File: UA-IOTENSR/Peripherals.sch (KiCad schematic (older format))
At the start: 4 parts, among them IC1 LM3914VX_NOPB, U4 SCD4X

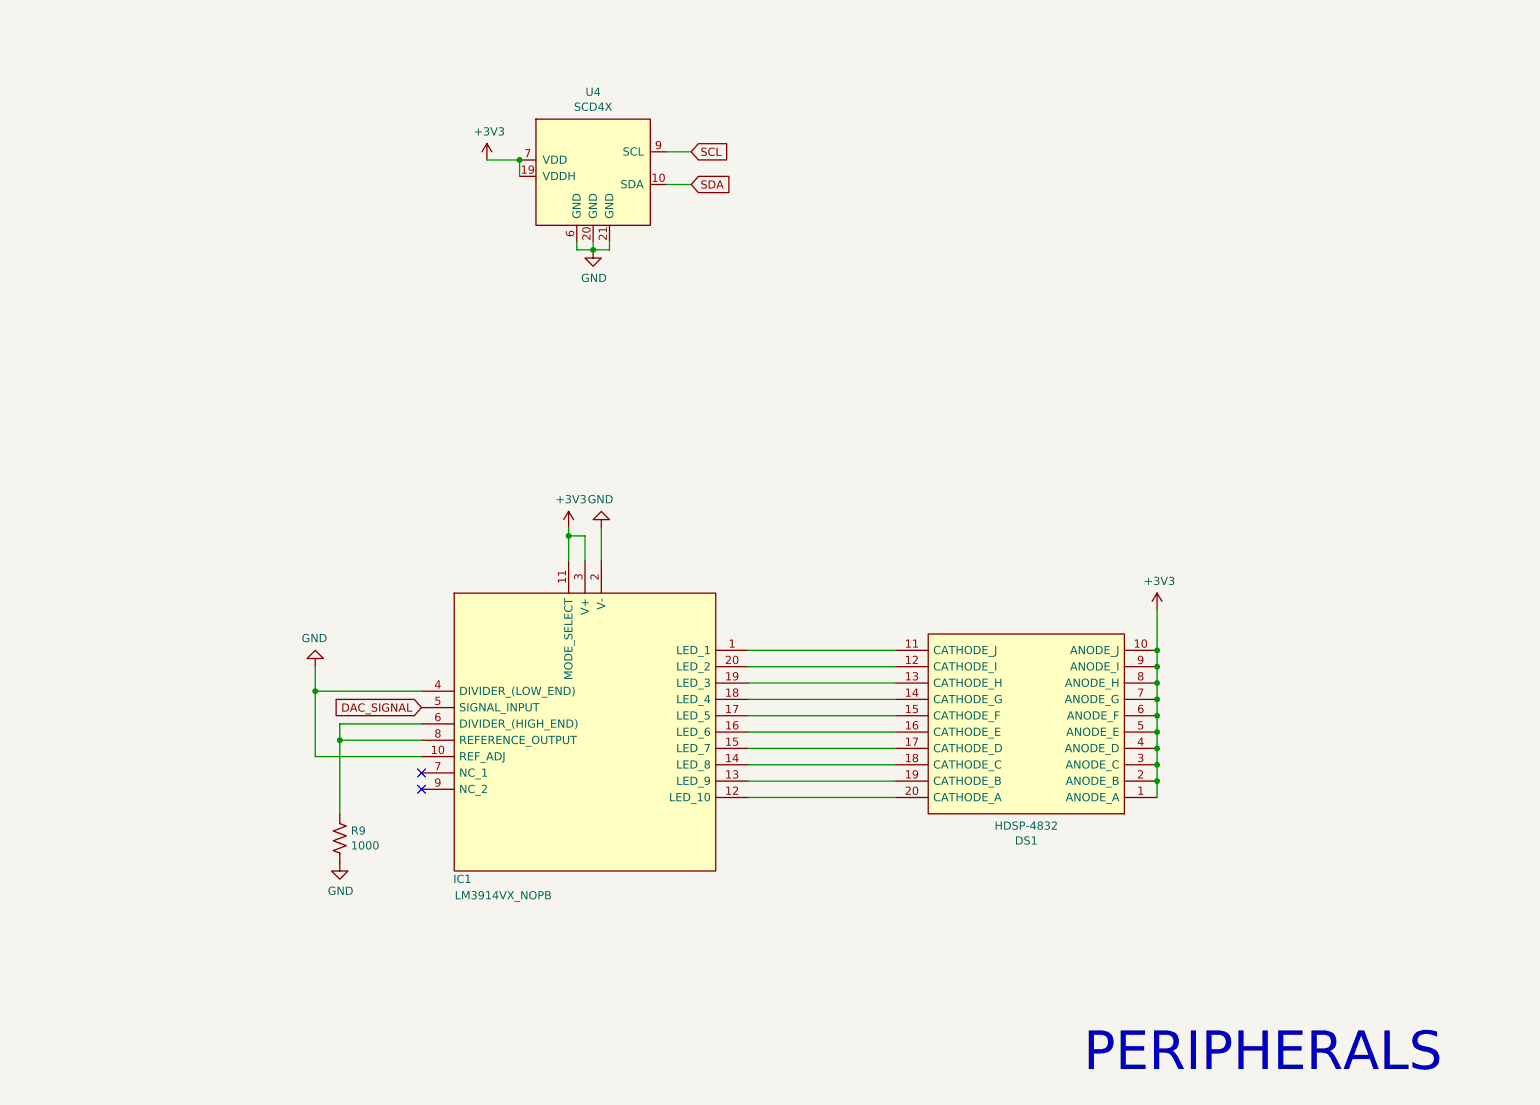
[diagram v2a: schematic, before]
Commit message: Made Peripheral sheet more pretty
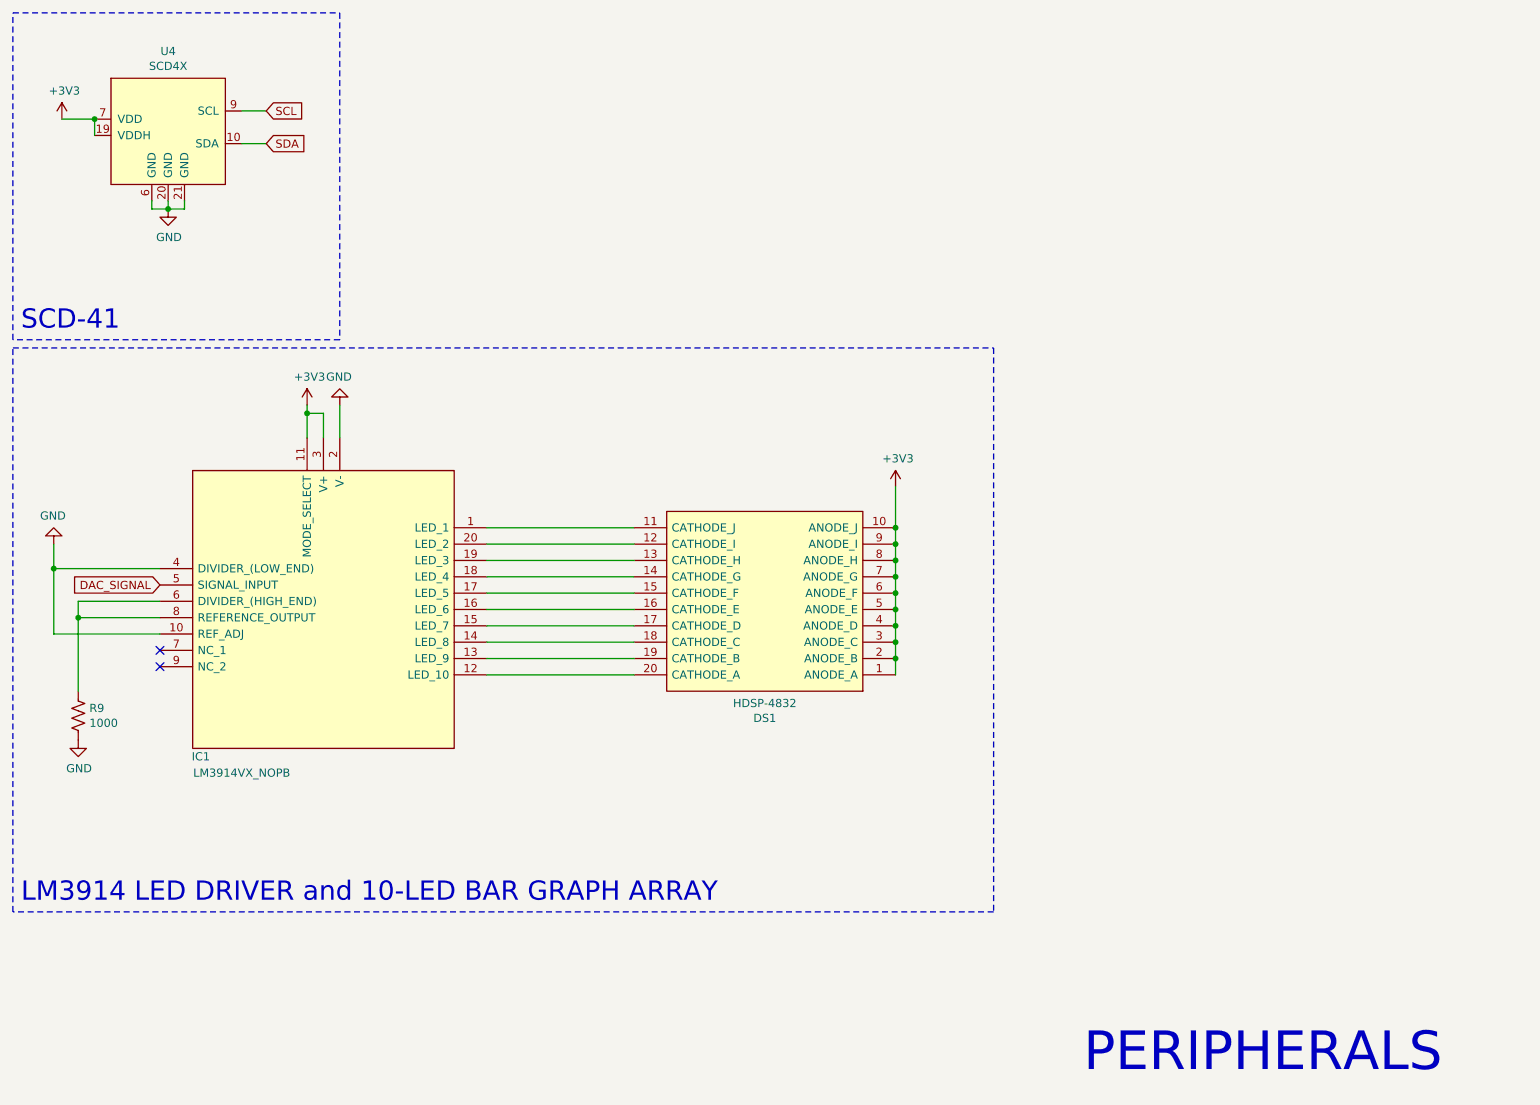
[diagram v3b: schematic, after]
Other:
- note added: "LM3914 LED DRIVER and 10-LED BAR GRAPH ARRAY"
- note added: "SCD-41"
- moved on the sheet: DS1, IC1, R9, U4

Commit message: Reassessed components
Removed bar graph led array and lm3914
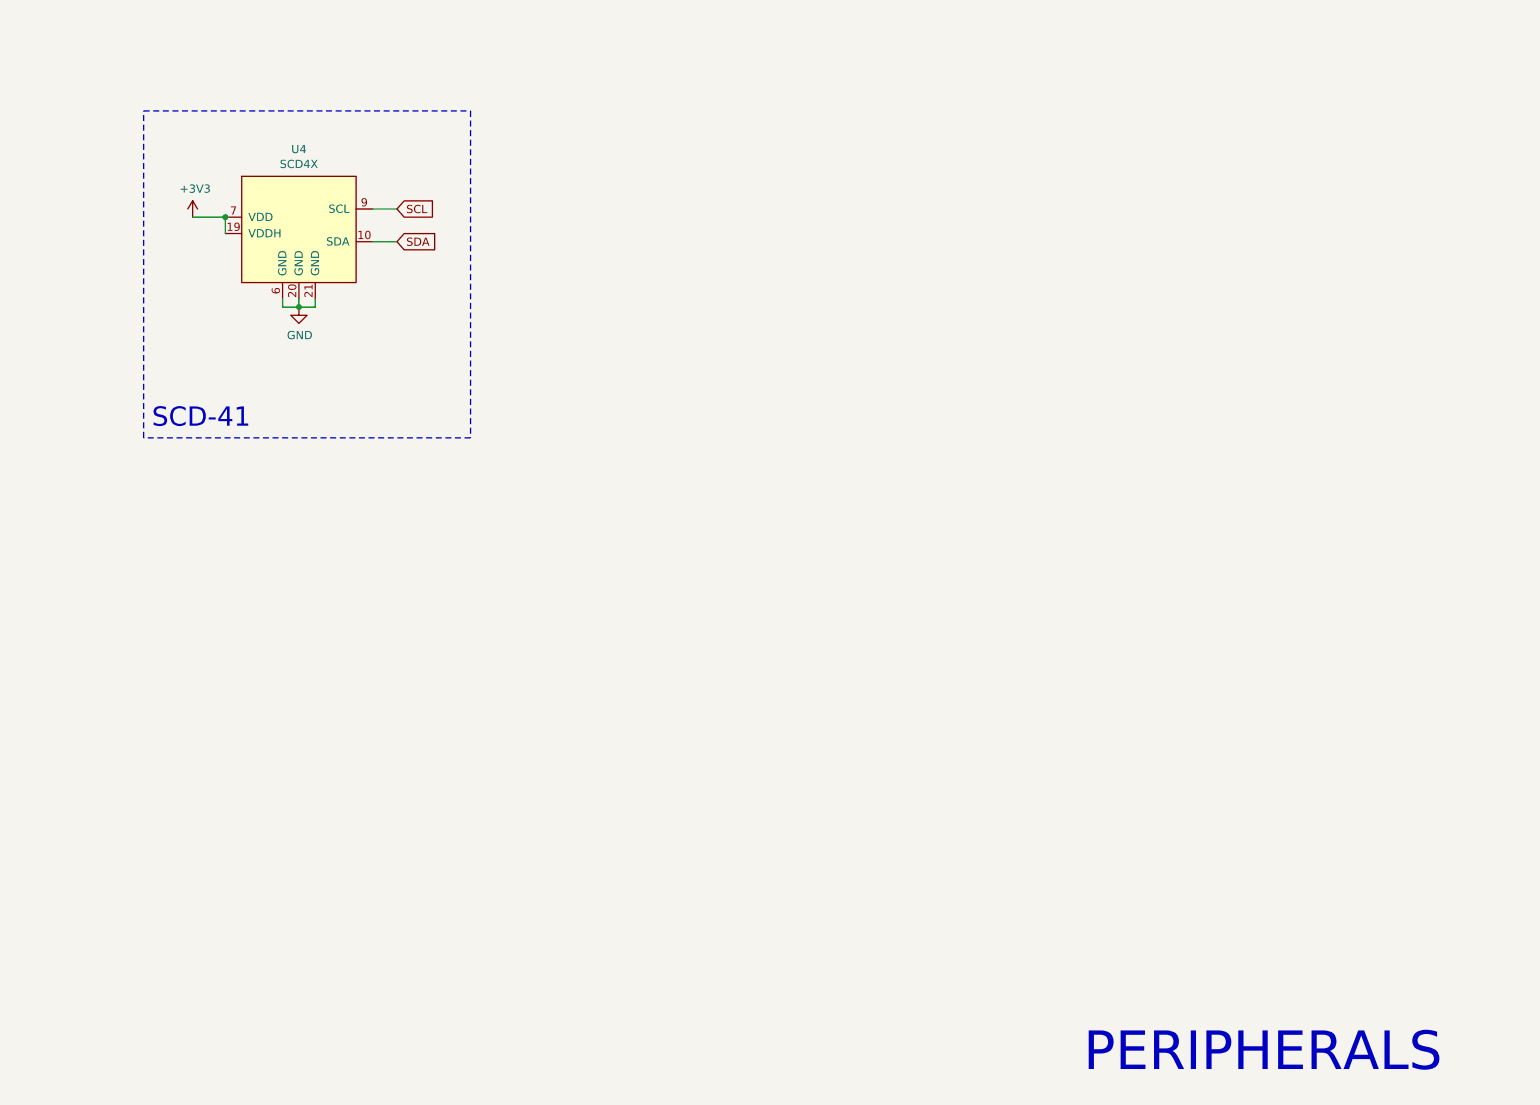
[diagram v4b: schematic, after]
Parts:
- removed DS1: HDSP-4832, DIPS762W61P254L2540H635Q20N, symbol UA-IOTENSR-rescue:HDSP-4832-Samacs
- removed IC1: LM3914VX_NOPB, PLCC127P990X990X457-20N, symbol UA-IOTENSR-rescue:LM3914VX_NOPB-Samacs
- removed R9: 1000, symbol Device:R_US
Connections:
- no-connect marks 2 -> 0
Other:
- note removed: "LM3914 LED DRIVER and 10-LED BAR GRAPH ARRAY"
- moved on the sheet: U4
